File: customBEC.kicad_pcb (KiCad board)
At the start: 2 copper layers, 40 x 40 mm, 24 parts, among them J18 ESC Logic Power, J19 Flight Controller Power, J3 Extra Header, J4 From Battery, U4 TPS5430DDA

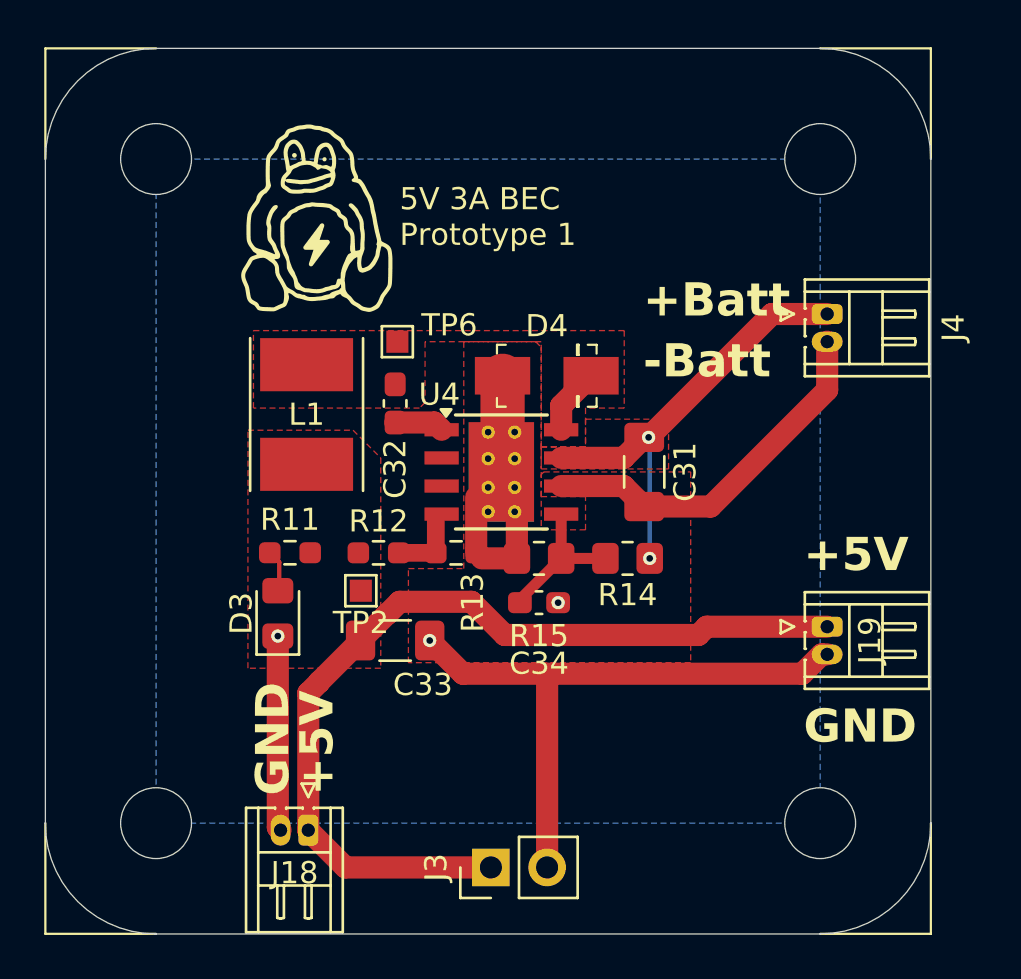
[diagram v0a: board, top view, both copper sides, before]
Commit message: Made Traces thicker for more power capabilities. i dunno if the vias can handle though
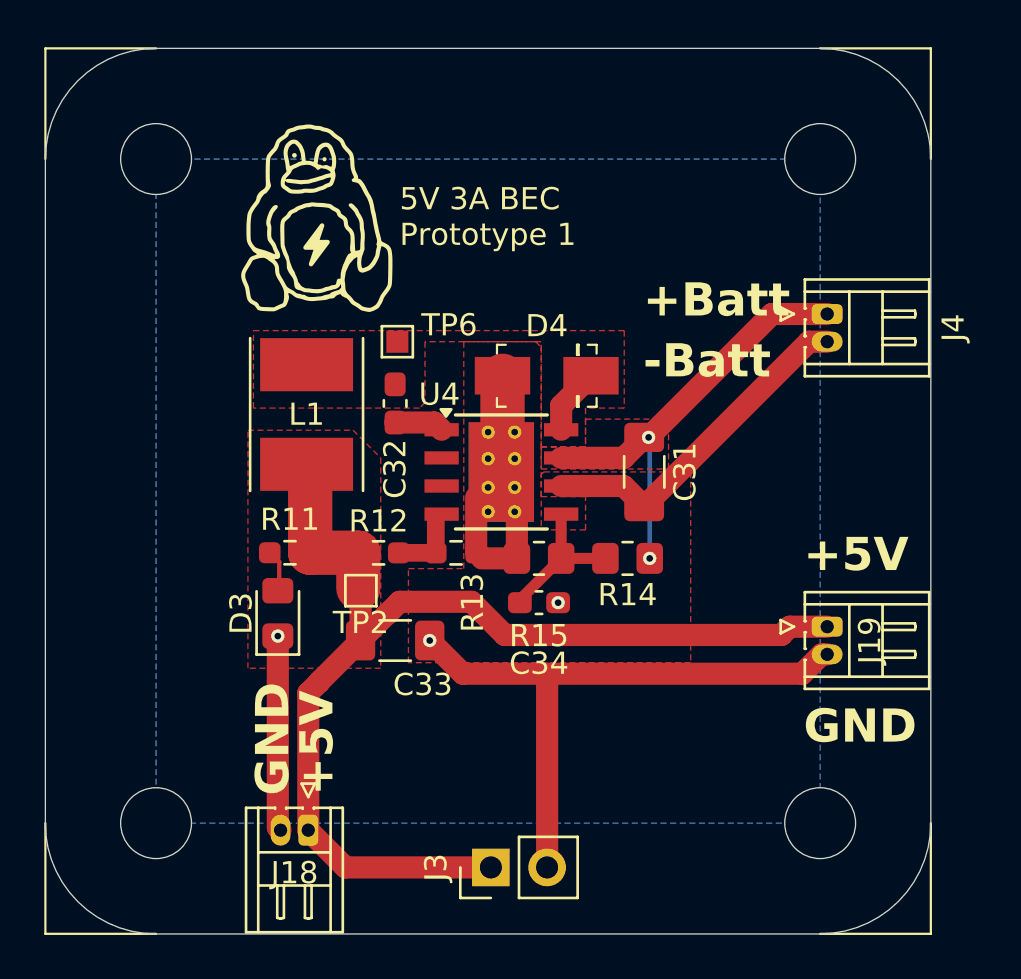
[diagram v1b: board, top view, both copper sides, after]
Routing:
- net BEC_OUT: track 41.1 -> 51.2 mm
- net BEC_GND: track 67.9 -> 66.6 mm
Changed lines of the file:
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@@
-	)
-	(segment
-		(start 60.3175 40.4325)
-		(end 55.0525 45.6975)
-		(width 1)
-		(layer "F.Cu")
-		(net 1)
 	)
 	(segment
@@
 	)
 	(segment
+		(start 59.4975 38.25)
+		(end 52.05 45.6975)
+		(width 1)
+		(layer "F.Cu")
+		(net 1)
+	)
+	(segment
 		(start 45.65 44.085)
 		(end 45.6 44.135)
@@
 	)
 	(segment
-		(start 55.0525 45.6975)
-		(end 52.05 45.6975)
-		(width 1)
-		(layer "F.Cu")
-		(net 1)
-	)
-	(segment
 		(start 60.0675 52.375)
 		(end 59.1925 53.25)
@@
 	)
 	(segment
+		(start 60.3175 38.25)
+		(end 59.4975 38.25)
+		(width 1)
+		(layer "F.Cu")
+		(net 1)
+	)
+	(segment
 		(start 43.8625 53.25)
 		(end 42.3625 51.75)
@@
 	)
 	(segment
-		(start 60.3175 38.25)
-		(end 60.3175 40.4325)
-		(width 1)
-		(layer "F.Cu")
-		(net 1)
-	)
-	(segment
 		(start 35.625 60.3175)
 		(end 35.5 60.1925)
@@
 	)
 	(segment
-		(start 54.875 51.125)
-		(end 54.5 51.5)
+		(start 58.25 51.5)
+		(end 45.75 51.5)
+		(width 1)
+		(layer "F.Cu")
+		(net 5)
+	)
+	(segment
+		(start 60.3175 51.125)
+		(end 58.625 51.125)
+		(width 1)
+		(layer "F.Cu")
+		(net 5)
+	)
+	(segment
+		(start 39.2375 51.75)
+		(end 39.2375 49.5125)
+		(width 1)
+		(layer "F.Cu")
+		(net 5)
+	)
+	(segment
+		(start 45.75 51.5)
+		(end 44.25 50)
+		(width 1)
+		(layer "F.Cu")
+		(net 5)
+	)
+	(segment
+		(start 41 50)
+		(end 40.451 50.549)
 		(width 1)
 		(layer "F.Cu")
@@
 	)
 	(segment
-		(start 54.5 51.5)
-		(end 45.75 51.5)
+		(start 44.25 50)
+		(end 41 50)
 		(width 1)
 		(layer "F.Cu")
@@
 	)
 	(segment
+		(start 39.1325 47.785)
+		(end 39.1375 47.79)
+		(width 2)
+		(layer "F.Cu")
+		(net 5)
+	)
+	(segment
+		(start 36.9625 47.785)
+		(end 36.9625 43.9525)
+		(width 2)
+		(layer "F.Cu")
+		(net 5)
+	)
+	(segment
 		(start 40.451 50.549)
 		(end 40.4385 50.549)
@@
 	)
 	(segment
+		(start 37.3625 53.6375)
+		(end 36.875 54.125)
+		(width 1)
+		(layer "F.Cu")
+		(net 5)
+	)
+	(segment
+		(start 58.625 51.125)
+		(end 58.25 51.5)
+		(width 1)
+		(layer "F.Cu")
+		(net 5)
+	)
+	(segment
+		(start 36.9625 47.785)
+		(end 39.1325 47.785)
+		(width 2)
+		(layer "F.Cu")
+		(net 5)
+	)
+	(segment
+		(start 36.875 54.125)
+		(end 36.875 60.3175)
+		(width 1)
+		(layer "F.Cu")
+		(net 5)
+	)
+	(segment
+		(start 39.1375 47.79)
+		(end 39.1375 49.3875)
+		(width 2)
+		(layer "F.Cu")
+		(net 5)
+	)
+	(segment
 		(start 40.4385 50.549)
 		(end 39.2375 51.75)
@@
 	)
 	(segment
-		(start 37.3625 53.6375)
-		(end 36.875 54.125)
-		(width 1)
-		(layer "F.Cu")
-		(net 5)
-	)
-	(segment
-		(start 44.25 50)
-		(end 41 50)
-		(width 1)
-		(layer "F.Cu")
-		(net 5)
-	)
-	(segment
-		(start 36.875 54.125)
-		(end 36.875 60.3175)
-		(width 1)
-		(layer "F.Cu")
-		(net 5)
-	)
-	(segment
 		(start 45.125 62)
 		(end 38.5575 62)
@@
 	)
 	(segment
-		(start 41 50)
-		(end 40.451 50.549)
-		(width 1)
-		(layer "F.Cu")
-		(net 5)
-	)
-	(segment
-		(start 45.75 51.5)
-		(end 44.25 50)
+		(start 39.2375 49.5125)
+		(end 39.25 49.5)
 		(width 1)
 		(layer "F.Cu")
@@
 	)
 	(segment
-		(start 60.3175 51.125)
-		(end 54.875 51.125)
-		(width 1)
-		(layer "F.Cu")
-		(net 5)
+		(start 36.9625 43.9525)
+		(end 36.8 43.79)
+		(width 0.2)
+		(layer "F.Cu")
+		(net 5)

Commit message: re-annotate and fix drc issues
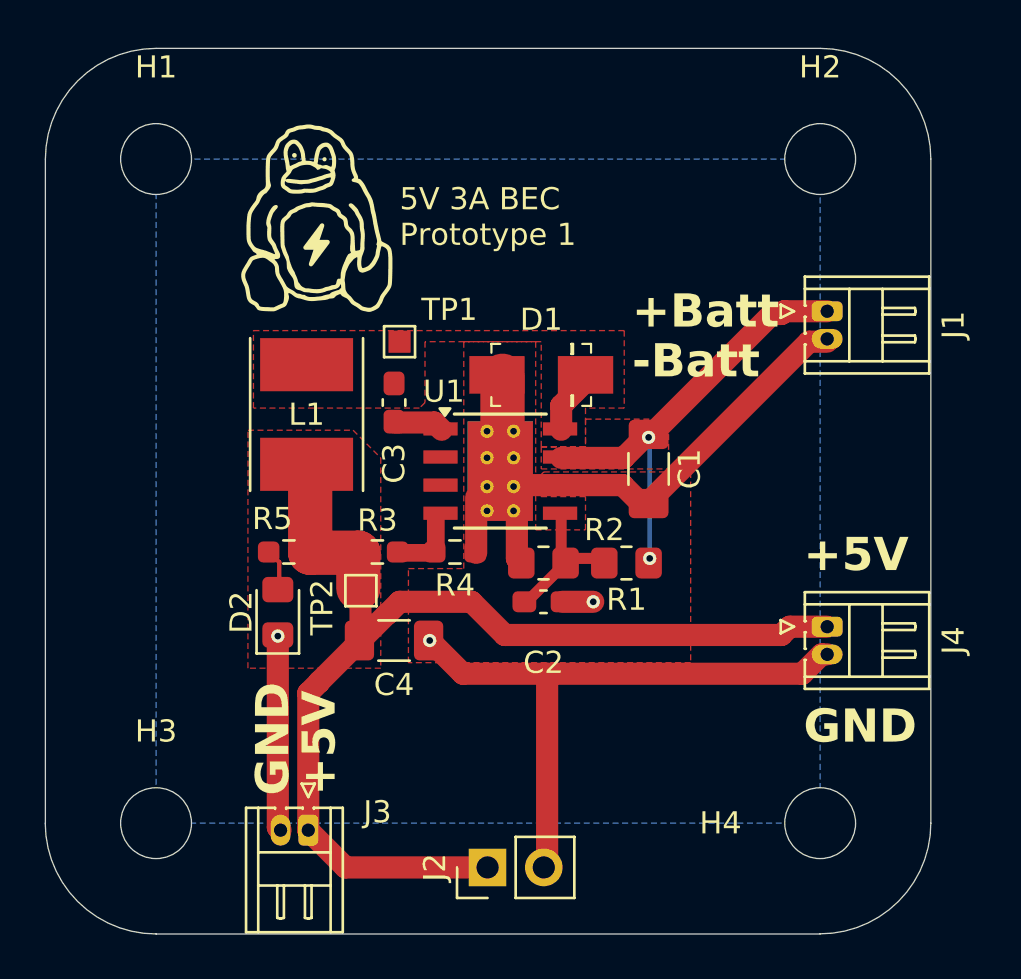
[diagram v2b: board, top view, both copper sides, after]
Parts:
- removed C31: 10uF, Capacitor_SMD:C_1206_3216Metric_Pad1.33x1.80mm_HandSolder
- removed C32, C34: 10nF, Capacitor_SMD:C_0603_1608Metric_Pad1.08x0.95mm_HandSolder
- removed C33: 220uF, Capacitor_SMD:C_1206_3216Metric_Pad1.33x1.80mm_HandSolder
- removed D3: 5V LED, LED_SMD:LED_0805_2012Metric_Pad1.15x1.40mm_HandSolder
- removed D4: B340A, digikey-footprints:DO-214AC
- removed J18: ESC Logic Power, Connector_Hirose:Hirose_DF13-02P-1.25DS_1x02_P1.25mm_Horizontal
- removed J19: Flight Controller Power, Connector_Hirose:Hirose_DF13-02P-1.25DS_1x02_P1.25mm_Horizontal
- removed R11: 10K, Resistor_SMD:R_0603_1608Metric_Pad0.98x0.95mm_HandSolder
- removed R12: 10k, Resistor_SMD:R_0603_1608Metric_Pad0.98x0.95mm_HandSolder
- removed R13: 3.24k, Resistor_SMD:R_0603_1608Metric_Pad0.98x0.95mm_HandSolder
- removed R14: 100k, Resistor_SMD:R_0805_2012Metric_Pad1.20x1.40mm_HandSolder
- removed R15: 18k, Resistor_SMD:R_0805_2012Metric_Pad1.20x1.40mm_HandSolder
- removed REF** (x4): MountingHole_3.2mm_M3, MountingHole:MountingHole_3.2mm_M3
- removed TP6: Per datasheet, TestPoint:TestPoint_Pad_1.0x1.0mm
- removed U4: TPS5430DDA, Package_SO:TI_SO-PowerPAD-8_ThermalVias
- added C1: 10uF, Capacitor_SMD:C_1206_3216Metric_Pad1.33x1.80mm_HandSolder, F.Cu at (52.2, 44.0)
- added C2: 10nF, Capacitor_SMD:C_0603_1608Metric_Pad1.08x0.95mm_HandSolder, F.Cu at (47.5, 50.0)
- added C3: 10nF, Capacitor_SMD:C_0603_1608Metric_Pad1.08x0.95mm_HandSolder, F.Cu at (40.8, 41.0)
- added C4: 220uF, Capacitor_SMD:C_1206_3216Metric_Pad1.33x1.80mm_HandSolder, F.Cu at (40.8, 51.8)
- added D1: B340A, digikey-footprints:DO-214AC, F.Cu at (47.4, 39.8)
- added D2: 5V LED, LED_SMD:LED_0805_2012Metric_Pad1.15x1.40mm_HandSolder, F.Cu at (35.5, 50.5)
- added H1: MountingHole, MountingHole:MountingHole_3.2mm_M3, F.Cu at (30.0, 30.0)
- added H2: MountingHole, MountingHole:MountingHole_3.2mm_M3, F.Cu at (60.0, 30.0)
- added H3: MountingHole, MountingHole:MountingHole_3.2mm_M3, F.Cu at (30.0, 60.0)
- added H4: MountingHole, MountingHole:MountingHole_3.2mm_M3, F.Cu at (60.0, 60.0)
- added J1: From Battery, Connector_Hirose:Hirose_DF13-02P-1.25DS_1x02_P1.25mm_Horizontal, F.Cu at (60.3, 36.9)
- added J2: Extra Header, Connector_PinHeader_2.54mm:PinHeader_1x02_P2.54mm_Vertical, F.Cu at (45.0, 62.0)
- added R1: 100k, Resistor_SMD:R_0805_2012Metric_Pad1.20x1.40mm_HandSolder, F.Cu at (51.2, 48.2)
- added R2: 18k, Resistor_SMD:R_0805_2012Metric_Pad1.20x1.40mm_HandSolder, F.Cu at (47.5, 48.2)
- added R3: 10k, Resistor_SMD:R_0603_1608Metric_Pad0.98x0.95mm_HandSolder, F.Cu at (40.0, 47.8)
- added R4: 3.24k, Resistor_SMD:R_0603_1608Metric_Pad0.98x0.95mm_HandSolder, F.Cu at (43.5, 47.8)
- added R5: 10K, Resistor_SMD:R_0603_1608Metric_Pad0.98x0.95mm_HandSolder, F.Cu at (36.0, 47.8)
- added TP1: Per datasheet, TestPoint:TestPoint_Pad_1.0x1.0mm, F.Cu at (41.0, 38.2)
- added U1: TPS5430DDA, Package_SO:TI_SO-PowerPAD-8_ThermalVias, F.Cu at (45.5, 44.1)
- J3: value Extra Header -> ESC Logic Power; footprint Connector_PinHeader_2.54mm:PinHeader_1x02_P2.54mm_Vertical -> Connector_Hirose:Hirose_DF13-02P-1.25DS_1x02_P1.25mm_Horizontal
- J4: value From Battery -> Flight Controller Power
- moved J4 14.1 mm to (60.3, 51.1)
- moved J3 8.42 mm to (36.9, 60.3), turned to 180 degrees
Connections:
- J4 pad 1: BEC_VIN -> BEC_OUT
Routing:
- net Net-(U4-EN): track 6.77 -> 0.00 mm
- net Net-(U1-EN): track 0.00 -> 6.19 mm
- net Net-(U4-VSENSE): track 3.53 -> 0.00 mm
- net Net-(U1-VSENSE): track 0.00 -> 3.53 mm
- net BEC_GND: track 66.6 -> 68.9 mm
- net Net-(U4-BOOT): track 2.24 -> 0.00 mm
- net Net-(U1-BOOT): track 0.00 -> 2.24 mm
- net Net-(D3-A): track 1.68 -> 0.00 mm
- net Net-(D2-A): track 0.00 -> 1.68 mm
